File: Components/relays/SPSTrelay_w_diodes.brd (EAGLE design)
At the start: 11.1 x 30.5 mm, 3 parts, among them K2 HF41F-12-H

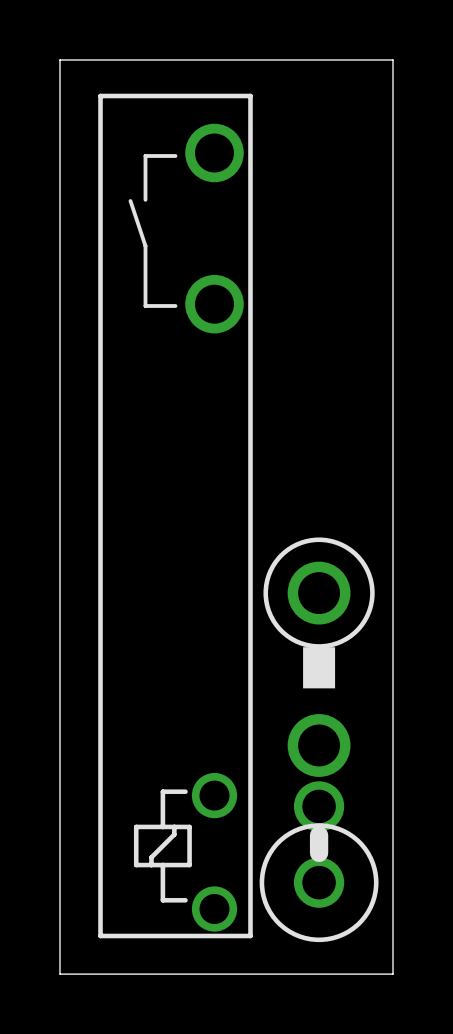
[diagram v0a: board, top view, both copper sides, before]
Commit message: Correcting footprint for SPST and SPDT relays
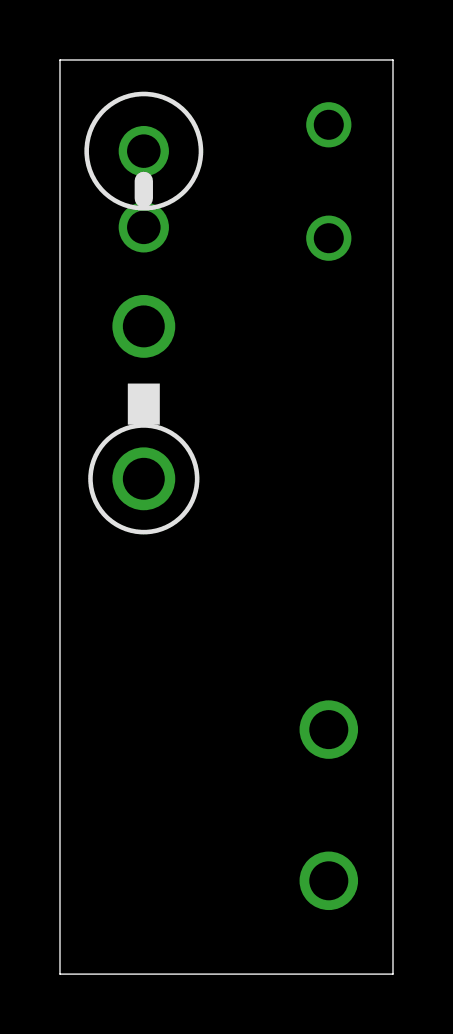
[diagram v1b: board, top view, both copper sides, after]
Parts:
- removed K2: HF41F-12-H, relay_computer_custom:HF41F-12-H
- added K1: HF41F-12-H, relay_computer_custom:HF41F-12-H
- moved D1 22.6 mm to (2.79, 26.2), turned to 270 degrees
- moved D2 10.6 mm to (2.79, 19.1), turned to 90 degrees
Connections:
- net GND: now also K1.2; no longer K2.2
- net IN: now also K1.1; no longer K2.1
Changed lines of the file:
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@@
 <?xml version="1.0" encoding="utf-8"?>
 <!DOCTYPE eagle SYSTEM "eagle.dtd">
-<eagle version="8.3.2">
+<eagle version="8.7.0">
 <drawing>
 <settings>
@@
 <layers>
 <layer number="1" name="Top" color="4" fill="1" visible="yes" active="yes"/>
+<layer number="2" name="Route2" color="1" fill="3" visible="no" active="no"/>
+<layer number="15" name="Route15" color="4" fill="6" visible="no" active="no"/>
 <layer number="16" name="Bottom" color="1" fill="1" visible="yes" active="yes"/>
 <layer number="17" name="Pads" color="2" fill="1" visible="yes" active="yes"/>
@@
 <param name="dpMaxLengthDifference" value="10mm"/>
 <param name="dpGapFactor" value="2.5"/>
-<param name="checkGrid" value="0"/>
 <param name="checkAngle" value="0"/>
 <param name="checkFont" value="1"/>
 <param name="checkRestrict" value="1"/>
+<param name="checkStop" value="0"/>
+<param name="checkValues" value="0"/>
 <param name="useDiameter" value="13"/>
 <param name="maxErrors" value="50"/>
@@
 </autorouter>
 <elements>
-<element name="D1" library="relay_computer_custom" package="RAD2,5" value="1N4007" x="8.636" y="4.318" rot="R90"/>
-<element name="D2" library="relay_computer_custom" package="C1702-05" value="1N5359" x="8.636" y="10.16" rot="R270"/>
-<element name="K2" library="relay_computer_custom" package="HF41F-12-H" value="HF41F-12-H" x="6.35" y="1.27" rot="R90"/>
+<element name="D1" library="relay_computer_custom" package="RAD2,5" value="1N4007" x="2.794" y="26.162" rot="R270"/>
+<element name="D2" library="relay_computer_custom" package="C1702-05" value="1N5359" x="2.794" y="19.05" rot="R90"/>
+<element name="K1" library="relay_computer_custom" package="HF41F-12-H" value="HF41F-12-H" x="10.16" y="1.27" rot="R90"/>
 </elements>
 <signals>
@@
 <contactref element="D1" pad="A"/>
 <contactref element="D2" pad="A"/>
-<wire x1="8.636" y1="5.588" x2="8.636" y2="7.62" width="0" layer="19" extent="1-1"/>
+<wire x1="2.794" y1="24.892" x2="2.794" y2="21.59" width="0" layer="19" extent="1-1"/>
 </signal>
 <signal name="GND">
 <contactref element="D2" pad="C"/>
-<contactref element="K2" pad="2"/>
-<wire x1="5.15" y1="5.95" x2="8.636" y2="12.7" width="0" layer="19" extent="1-1"/>
+<contactref element="K1" pad="2"/>
+<wire x1="8.96" y1="24.53" x2="2.794" y2="16.51" width="0" layer="19" extent="1-1"/>
 </signal>
 <signal name="IN">
 <contactref element="D1" pad="C"/>
-<contactref element="K2" pad="1"/>
-<wire x1="5.15" y1="2.17" x2="8.636" y2="3.048" width="0" layer="19" extent="1-1"/>
+<contactref element="K1" pad="1"/>
+<wire x1="2.794" y1="27.432" x2="8.96" y2="28.31" width="0" layer="19" extent="1-1"/>
 </signal>
 </signals>

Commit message: Updating components with latest library updates
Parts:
- D2: value 1N5359 -> 1N5359VERT_SML; device relay_computer_custom:C1702-05 -> relay_computer_custom:RAD2.5_D2
- moved D2 2.54 mm to (2.79, 21.6)
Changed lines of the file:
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@@
 <layer number="48" name="Document" color="7" fill="1" visible="yes" active="yes"/>
 <layer number="49" name="Reference" color="7" fill="1" visible="yes" active="yes"/>
+<layer number="50" name="dxf" color="7" fill="1" visible="no" active="no"/>
 <layer number="51" name="tDocu" color="7" fill="1" visible="yes" active="yes"/>
 <layer number="52" name="bDocu" color="7" fill="1" visible="yes" active="yes"/>
+<layer number="53" name="tGND_GNDA" color="7" fill="9" visible="no" active="no"/>
+<layer number="54" name="bGND_GNDA" color="1" fill="9" visible="no" active="no"/>
+<layer number="56" name="wert" color="7" fill="1" visible="no" active="no"/>
+<layer number="57" name="tCAD" color="7" fill="1" visible="no" active="no"/>
+<layer number="59" name="tCarbon" color="7" fill="1" visible="no" active="no"/>
+<layer number="60" name="bCarbon" color="7" fill="1" visible="no" active="no"/>
 <layer number="90" name="Modules" color="5" fill="1" visible="no" active="no"/>
 <layer number="91" name="Nets" color="2" fill="1" visible="no" active="no"/>
@@
 <layer number="98" name="Guide" color="6" fill="1" visible="no" active="no"/>
 <layer number="99" name="SpiceOrder" color="5" fill="1" visible="no" active="no"/>
+<layer number="100" name="Muster" color="7" fill="1" visible="no" active="no"/>
+<layer number="101" name="Patch_Top" color="12" fill="4" visible="no" active="yes"/>
+<layer number="102" name="Vscore" color="7" fill="1" visible="no" active="yes"/>
+<layer number="103" name="fp3" color="7" fill="1" visible="no" active="yes"/>
+<layer number="104" name="Name" color="7" fill="1" visible="no" active="yes"/>
+<layer number="105" name="Beschreib" color="9" fill="1" visible="no" active="yes"/>
+<layer number="106" name="BGA-Top" color="4" fill="1" visible="no" active="yes"/>
+<layer number="107" name="BD-Top" color="5" fill="1" visible="no" active="yes"/>
+<layer number="108" name="fp8" color="7" fill="1" visible="no" active="yes"/>
+<layer number="109" name="fp9" color="7" fill="1" visible="no" active="yes"/>
+<layer number="110" name="fp0" color="7" fill="1" visible="no" active="yes"/>
+<layer number="111" name="LPC17xx" color="7" fill="1" visible="no" active="yes"/>
+<layer number="112" name="tSilk" color="7" fill="1" visible="no" active="yes"/>
+<layer number="113" name="ReferenceLS" color="7" fill="1" visible="no" active="no"/>
+<layer number="114" name="Badge_Outline" color="7" fill="1" visible="no" active="yes"/>
+<layer number="115" name="ReferenceISLANDS" color="7" fill="1" visible="no" active="yes"/>
+<layer number="116" name="Patch_BOT" color="9" fill="4" visible="no" active="yes"/>
+<layer number="118" name="Rect_Pads" color="7" fill="1" visible="no" active="no"/>
+<layer number="121" name="_tsilk" color="7" fill="1" visible="no" active="yes"/>
+<layer number="122" name="_bsilk" color="7" fill="1" visible="no" active="yes"/>
+<layer number="123" name="tTestmark" color="7" fill="1" visible="no" active="yes"/>
+<layer number="124" name="bTestmark" color="7" fill="1" visible="no" active="yes"/>
+<layer number="125" name="_tNames" color="7" fill="1" visible="no" active="yes"/>
+<layer number="126" name="_bNames" color="7" fill="1" visible="no" active="yes"/>
+<layer number="127" name="_tValues" color="7" fill="1" visible="no" active="yes"/>
+<layer number="128" name="_bValues" color="7" fill="1" visible="no" active="yes"/>
+<layer number="129" name="Mask" color="7" fill="1" visible="no" active="yes"/>
+<layer number="131" name="tAdjust" color="7" fill="1" visible="no" active="yes"/>
+<layer number="132" name="bAdjust" color="7" fill="1" visible="no" active="yes"/>
+<layer number="144" name="Drill_legend" color="7" fill="1" visible="no" active="yes"/>
+<layer number="150" name="Notes" color="7" fill="1" visible="no" active="yes"/>
+<layer number="151" name="HeatSink" color="7" fill="1" visible="no" active="yes"/>
+<layer number="152" name="_bDocu" color="7" fill="1" visible="no" active="yes"/>
+<layer number="153" name="FabDoc1" color="6" fill="1" visible="no" active="no"/>
+<layer number="154" name="FabDoc2" color="2" fill="1" visible="no" active="no"/>
+<layer number="155" name="FabDoc3" color="7" fill="15" visible="no" active="no"/>
+<layer number="199" name="Contour" color="7" fill="1" visible="no" active="yes"/>
+<layer number="200" name="200bmp" color="1" fill="10" visible="no" active="yes"/>
+<layer number="201" name="201bmp" color="2" fill="1" visible="no" active="no"/>
+<layer number="202" name="202bmp" color="3" fill="1" visible="no" active="no"/>
+<layer number="203" name="203bmp" color="4" fill="10" visible="no" active="yes"/>
+<layer number="204" name="204bmp" color="5" fill="10" visible="no" active="yes"/>
+<layer number="205" name="205bmp" color="6" fill="10" visible="no" active="yes"/>
+<layer number="206" name="206bmp" color="7" fill="10" visible="no" active="yes"/>
+<layer number="207" name="207bmp" color="8" fill="10" visible="no" active="yes"/>
+<layer number="208" name="208bmp" color="9" fill="10" visible="no" active="yes"/>
+<layer number="209" name="209bmp" color="7" fill="1" visible="no" active="yes"/>
+<layer number="210" name="210bmp" color="7" fill="1" visible="no" active="yes"/>
+<layer number="211" name="211bmp" color="7" fill="1" visible="no" active="yes"/>
+<layer number="212" name="212bmp" color="7" fill="1" visible="no" active="yes"/>
+<layer number="213" name="213bmp" color="7" fill="1" visible="no" active="yes"/>
+<layer number="214" name="214bmp" color="7" fill="1" visible="no" active="yes"/>
+<layer number="215" name="215bmp" color="7" fill="1" visible="no" active="yes"/>
+<layer number="216" name="216bmp" color="7" fill="1" visible="no" active="yes"/>
+<layer number="217" name="217bmp" color="18" fill="1" visible="no" active="no"/>
+<layer number="218" name="218bmp" color="19" fill="1" visible="no" active="no"/>
+<layer number="219" name="219bmp" color="20" fill="1" visible="no" active="no"/>
+<layer number="220" name="220bmp" color="21" fill="1" visible="no" active="no"/>
+<layer number="221" name="221bmp" color="22" fill="1" visible="no" active="no"/>
+<layer number="222" name="222bmp" color="23" fill="1" visible="no" active="no"/>
+<layer number="223" name="223bmp" color="24" fill="1" visible="no" active="no"/>
+<layer number="224" name="224bmp" color="25" fill="1" visible="no" active="no"/>
+<layer number="225" name="225bmp" color="7" fill="1" visible="no" active="yes"/>
+<layer number="226" name="226bmp" color="7" fill="1" visible="no" active="yes"/>
+<layer number="227" name="227bmp" color="7" fill="1" visible="no" active="yes"/>
+<layer number="228" name="228bmp" color="7" fill="1" visible="no" active="yes"/>
+<layer number="229" name="229bmp" color="7" fill="1" visible="no" active="yes"/>
+<layer number="230" name="230bmp" color="7" fill="1" visible="no" active="yes"/>
+<layer number="231" name="Eagle3D_PG1" color="7" fill="1" visible="no" active="no"/>
+<layer number="232" name="Eagle3D_PG2" color="7" fill="1" visible="no" active="no"/>
+<layer number="233" name="Eagle3D_PG3" color="7" fill="1" visible="no" active="no"/>
+<layer number="248" name="Housing" color="7" fill="1" visible="no" active="yes"/>
+<layer number="249" name="Edge" color="7" fill="1" visible="no" active="yes"/>
+<layer number="250" name="Descript" color="7" fill="1" visible="no" active="no"/>
+<layer number="251" name="SMDround" color="7" fill="1" visible="no" active="no"/>
+<layer number="254" name="cooling" color="7" fill="1" visible="no" active="yes"/>
+<layer number="255" name="routoute" color="7" fill="1" visible="no" active="yes"/>
 </layers>
 <board>
@@
 <elements>
 <element name="D1" library="relay_computer_custom" package="RAD2,5" value="1N4007" x="2.794" y="26.162" rot="R270"/>
-<element name="D2" library="relay_computer_custom" package="C1702-05" value="1N5359" x="2.794" y="19.05" rot="R90"/>
+<element name="D2" library="relay_computer_custom" package="RAD2.5_D2" value="1N5359VERT_SML" x="2.794" y="21.59" rot="R90"/>
 <element name="K1" library="relay_computer_custom" package="HF41F-12-H" value="HF41F-12-H" x="10.16" y="1.27" rot="R90"/>
 </elements>
@@
 <contactref element="D1" pad="A"/>
 <contactref element="D2" pad="A"/>
-<wire x1="2.794" y1="24.892" x2="2.794" y2="21.59" width="0" layer="19" extent="1-1"/>
+<wire x1="2.794" y1="24.892" x2="2.794" y2="22.86" width="0" layer="19" extent="1-1"/>
 </signal>
 <signal name="GND">
 <contactref element="D2" pad="C"/>
 <contactref element="K1" pad="2"/>
-<wire x1="8.96" y1="24.53" x2="2.794" y2="16.51" width="0" layer="19" extent="1-1"/>
+<wire x1="8.96" y1="24.53" x2="2.794" y2="20.32" width="0" layer="19" extent="1-1"/>
 </signal>
 <signal name="IN">
